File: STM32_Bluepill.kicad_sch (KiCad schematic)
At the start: 10 parts

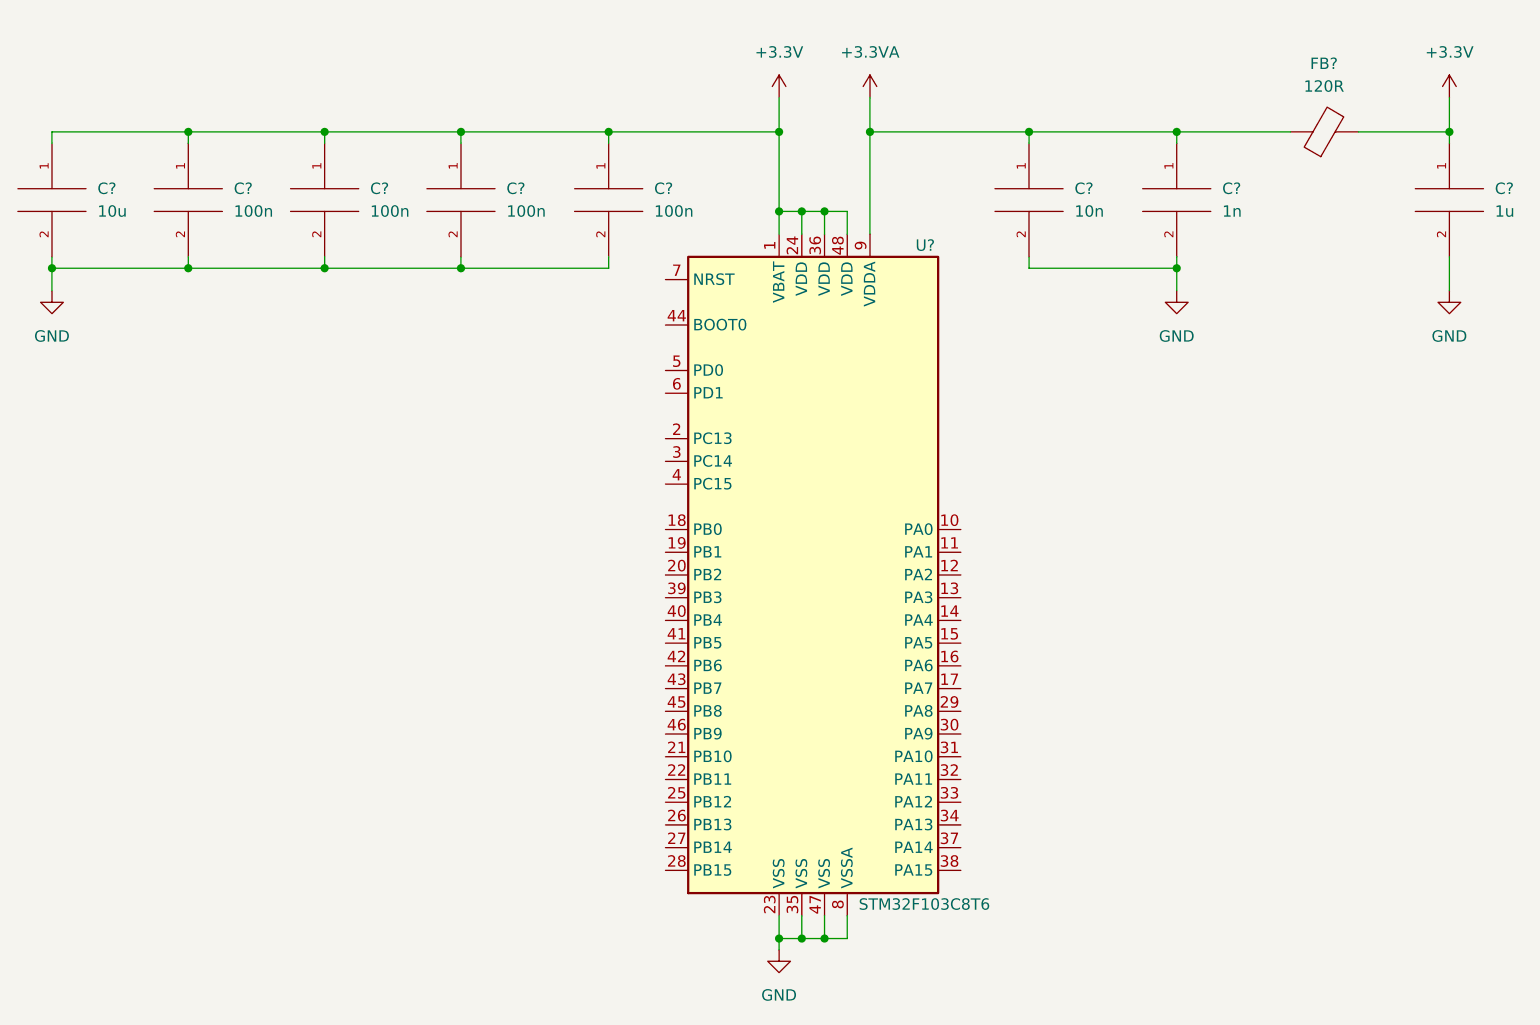
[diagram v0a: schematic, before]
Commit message: Schematic: Add Configuration pins NRST and BOOT0
	- Add a switch for BOOT0 to allow it to be programmed
	- NRST should already have an internal pullup
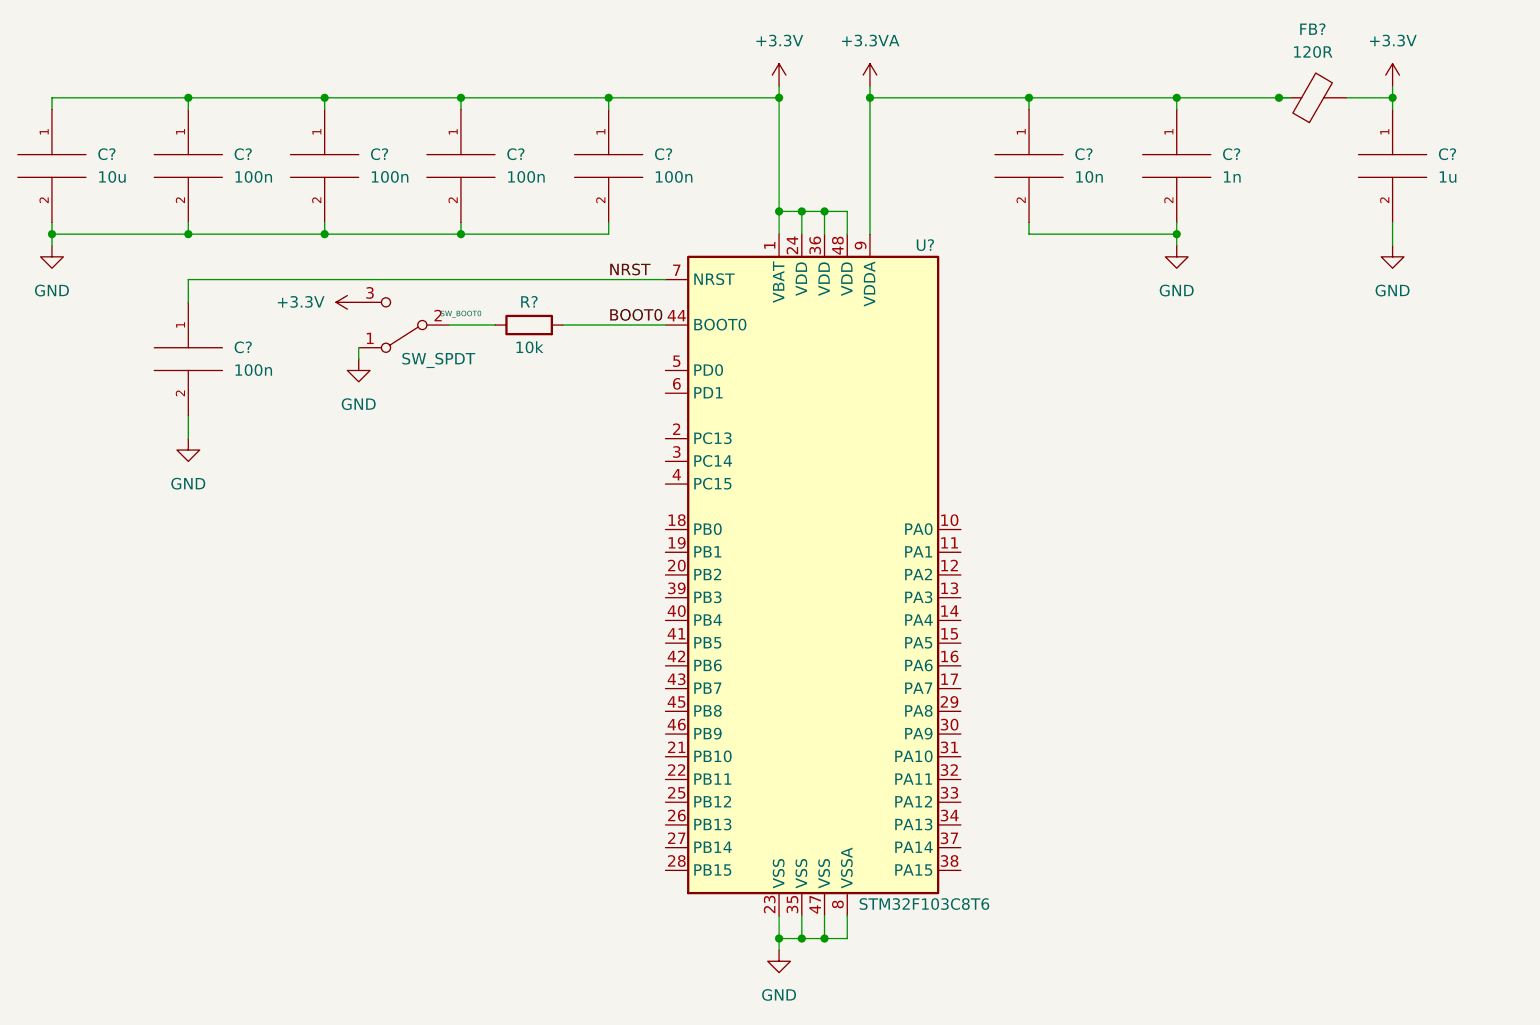
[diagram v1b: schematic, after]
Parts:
- added C?: 100n, symbol pspice:C
- added R?: 10k, symbol Device:R
- added SW_BOOT0: SW_SPDT, symbol Switch:SW_SPDT
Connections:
- net +3.3V: now also SW_BOOT0.3 (C)
- net GND: now also C?.2, SW_BOOT0.1 (A)
- net BOOT0: now reaches U?.44 (BOOT0)
- net BOOT0: now also R?.2
- net NRST: now reaches U?.7 (NRST)
- net NRST: now also C?.1
- new net: R?.1, SW_BOOT0.2 (B)
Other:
- moved on the sheet: C?, FB?
